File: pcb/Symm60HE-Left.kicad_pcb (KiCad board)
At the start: 2 copper layers, 155.5 x 106.4 mm, 124 parts

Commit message: Rename to Symm60HE; two-layer routing that is clean by construction
Rename every DOE60-* file and reference to Symm60HE-*, matching the repo.
The seven "DOE" mentions that remain are about the layout being reproduced,
which is correct.

Routing is now two layers with vias, at 0.2 mm trace / 0.15 mm clearance /
0.45 mm vias -- a rule chosen so the 0.5 mm grid's own diagonal spacing
(0.354 mm) satisfies it, and relaxed for any fabricator.

Three fixes, each of which was a real defect in the single-layer pass:

  * A diagonal step now requires both of its orthogonal neighbours.  Without
    it two nets cut the same gap from opposite corners and cross; cell
    ownership cannot see that, because neither net owns a cell the other
    used.  It was producing 49 shorts on the left half alone.
  * Fine-pitch pins are met head-on through a private escape lane along the
    pad's own axis, staggered near/far by pin parity.  A 0.65 mm TSSOP has
    0.25 mm between pads, so there is no side access at any rule; and without
    the lane the two neighbours' keep-out margins meet in front of a pin's
    tip and one of them owns the only way out.  The lane runs both ways,
    because an edge connector's contacts face off-board -- that is the way
    the cable goes in -- so its only exit is inwards under its own body.
  * Every route is rebuilt as real geometry and checked against everything
    already on the board before it is kept.  A route that would violate
    clearance is dropped and counted unrouted, so the files on disk are clean
    by construction and the honest number is the routed/unrouted split.

Left 143 of 156 connections, right 151 of 168, daughterboard 15 of 37.

Two things the checks were missing:

  * routecheck.py never tested trace-to-trace clearance, which is exactly
    what the diagonal crossings needed.  It does now, and it no longer counts
    a branch leaving its trunk at a T as a loose end.
  * The USB-C keep-out only existed in the image script -- nothin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
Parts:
- removed AMR1, AMR2, AMR3, AMR4: SN74LV4051A, DOE60_Project:AM1_TSSOP-16_4.4x5mm_P0.65mm
- removed CMR1, CMR2, CMR3, CMR4, CR10A, CR11A, CR12A, CR13A, CR14A, CR15A, CR16A, CR17A, CR18A, CR19A, CR1A, CR20A, CR21A, CR22A, CR23A, CR24A, CR25A, CR26A, CR27A, CR28A, CR29A, CR2A, CR30A, CR31A, CR32A, CR33A, CR34A, CR35A, CR36A, CR3A, CR4A, CR5A, CR6A, CR7A, CR8A, CR9A: 100n, DOE60_Project:C1_C_0402_1005Metric
- removed CR10B, CR11B, CR12B, CR13B, CR14B, CR15B, CR16B, CR17B, CR18B, CR19B, CR1B, CR20B, CR21B, CR22B, CR23B, CR24B, CR25B, CR26B, CR27B, CR28B, CR29B, CR2B, CR30B, CR31B, CR32B, CR33B, CR34B, CR35B, CR36B, CR3B, CR4B, CR5B, CR6B, CR7B, CR8B, CR9B: 4.7n, DOE60_Project:C1_C_0402_1005Metric
- removed HER1, HER10, HER12, HER13, HER14, HER15, HER16, HER17, HER19, HER2, HER20, HER21, HER22, HER23, HER24, HER27, HER28, HER29, HER3, HER30, HER32, HER34, HER5, HER6, HER7, HER8, HER9: MT9102ET, DOE60_Project:HE_KEY_1.00u
- removed HER11, HER31, HER33, HER35: MT9102ET, DOE60_Project:HE_KEY_1.50u
- removed HER18: MT9102ET, DOE60_Project:HE_KEY_1.75u
- removed HER25, HER36: MT9102ET, DOE60_Project:HE_KEY_2.25u
- removed HER26: MT9102ET, DOE60_Project:HE_KEY_1.25u
- removed HER4: MT9102ET, DOE60_Project:HE_KEY_2.00u
- removed JR1: FFC_12P, DOE60_Project:FFC_12P_1.00mm_TopContact
- removed MHR1, MHR2, MHR3, MHR4: M2, DOE60_Project:MountingHole_2.2mm_M2_Pad
- removed SR1, SR2, SR3: STAB_MX, DOE60_Project:STABILIZER_MX_2U
- added AML1: SN74LV4051A, Symm60HE_Project:AM1_TSSOP-16_4.4x5mm_P0.65mm, B.Cu at (23.8, 65.5)
- added AML2: SN74LV4051A, Symm60HE_Project:AM1_TSSOP-16_4.4x5mm_P0.65mm, B.Cu at (55.3, 65.0)
- added AML3: SN74LV4051A, Symm60HE_Project:AM1_TSSOP-16_4.4x5mm_P0.65mm, B.Cu at (91.3, 60.5)
- added AML4: SN74LV4051A, Symm60HE_Project:AM1_TSSOP-16_4.4x5mm_P0.65mm, B.Cu at (116.3, 59.0)
- added CL10A: 100n, Symm60HE_Project:C1_C_0402_1005Metric, B.Cu at (50.5, 21.7)
- added CL10B: 4.7n, Symm60HE_Project:C1_C_0402_1005Metric, B.Cu at (63.8, 35.5)
- added CL11A: 100n, Symm60HE_Project:C1_C_0402_1005Metric, B.Cu at (69.8, 21.7)
- added CL11B: 4.7n, Symm60HE_Project:C1_C_0402_1005Metric, B.Cu at (82.8, 35.7)
- added CL12A: 100n, Symm60HE_Project:C1_C_0402_1005Metric, B.Cu at (90.3, 22.1)
- added CL12B: 4.7n, Symm60HE_Project:C1_C_0402_1005Metric, B.Cu at (102.7, 36.6)
- added CL13A: 100n, Symm60HE_Project:C1_C_0402_1005Metric, B.Cu at (111.8, 23.5)
- added CL13B: 4.7n, Symm60HE_Project:C1_C_0402_1005Metric, B.Cu at (123.5, 38.6)
- added CL14A: 100n, Symm60HE_Project:C1_C_0402_1005Metric, B.Cu at (132.2, 25.7)
- added CL14B: 4.7n, Symm60HE_Project:C1_C_0402_1005Metric, B.Cu at (143.8, 40.9)
- added CL15A: 100n, Symm60HE_Project:C1_C_0402_1005Metric, B.Cu at (9.12, 40.7)
- added CL15B: 4.7n, Symm60HE_Project:C1_C_0402_1005Metric, B.Cu at (22.3, 54.5)
- added CL16A: 100n, Symm60HE_Project:C1_C_0402_1005Metric, B.Cu at (35.3, 40.7)
- added CL16B: 4.7n, Symm60HE_Project:C1_C_0402_1005Metric, B.Cu at (48.5, 54.5)
- added CL17A: 100n, Symm60HE_Project:C1_C_0402_1005Metric, B.Cu at (54.4, 40.7)
- added CL17B: 4.7n, Symm60HE_Project:C1_C_0402_1005Metric, B.Cu at (67.6, 54.5)
- added CL18A: 100n, Symm60HE_Project:C1_C_0402_1005Metric, B.Cu at (73.7, 40.8)
- added CL18B: 4.7n, Symm60HE_Project:C1_C_0402_1005Metric, B.Cu at (86.7, 54.8)
- added CL19A: 100n, Symm60HE_Project:C1_C_0402_1005Metric, B.Cu at (94.6, 41.4)
- added CL19B: 4.7n, Symm60HE_Project:C1_C_0402_1005Metric, B.Cu at (106.9, 56.0)
- added CL1A: 100n, Symm60HE_Project:C1_C_0402_1005Metric, B.Cu at (4.83, 2.62)
- added CL1B: 4.7n, Symm60HE_Project:C1_C_0402_1005Metric, B.Cu at (18.0, 16.4)
- added CL20A: 100n, Symm60HE_Project:C1_C_0402_1005Metric, B.Cu at (116.0, 43.0)
- added CL20B: 4.7n, Symm60HE_Project:C1_C_0402_1005Metric, B.Cu at (127.6, 58.1)
- added CL21A: 100n, Symm60HE_Project:C1_C_0402_1005Metric, B.Cu at (9.12, 59.8)
- added CL21B: 4.7n, Symm60HE_Project:C1_C_0402_1005Metric, B.Cu at (22.3, 73.6)
- added CL22A: 100n, Symm60HE_Project:C1_C_0402_1005Metric, B.Cu at (40.1, 59.8)
- added CL22B: 4.7n, Symm60HE_Project:C1_C_0402_1005Metric, B.Cu at (53.3, 73.6)
- added CL23A: 100n, Symm60HE_Project:C1_C_0402_1005Metric, B.Cu at (59.1, 59.8)
- added CL23B: 4.7n, Symm60HE_Project:C1_C_0402_1005Metric, B.Cu at (72.3, 73.6)
- added CL24A: 100n, Symm60HE_Project:C1_C_0402_1005Metric, B.Cu at (78.8, 59.9)
- added CL24B: 4.7n, Symm60HE_Project:C1_C_0402_1005Metric, B.Cu at (91.6, 74.1)
- added CL25A: 100n, Symm60HE_Project:C1_C_0402_1005Metric, B.Cu at (100.0, 60.7)
- added CL25B: 4.7n, Symm60HE_Project:C1_C_0402_1005Metric, B.Cu at (112.0, 75.5)
- added CL26A: 100n, Symm60HE_Project:C1_C_0402_1005Metric, B.Cu at (121.2, 62.6)
- added CL26B: 4.7n, Symm60HE_Project:C1_C_0402_1005Metric, B.Cu at (132.8, 77.8)
- added CL27A: 100n, Symm60HE_Project:C1_C_0402_1005Metric, B.Cu at (1.97, 78.8)
- added CL27B: 4.7n, Symm60HE_Project:C1_C_0402_1005Metric, B.Cu at (15.2, 92.6)
- added CL28A: 100n, Symm60HE_Project:C1_C_0402_1005Metric, B.Cu at (6.74, 78.8)
- added CL28B: 4.7n, Symm60HE_Project:C1_C_0402_1005Metric, B.Cu at (19.9, 92.6)
- added CL29A: 100n, Symm60HE_Project:C1_C_0402_1005Metric, B.Cu at (21.0, 78.8)
- added CL29B: 4.7n, Symm60HE_Project:C1_C_0402_1005Metric, B.Cu at (34.2, 92.6)
- added CL2A: 100n, Symm60HE_Project:C1_C_0402_1005Metric, B.Cu at (23.9, 2.62)
- added CL2B: 4.7n, Symm60HE_Project:C1_C_0402_1005Metric, B.Cu at (37.1, 16.4)
- added CL30A: 100n, Symm60HE_Project:C1_C_0402_1005Metric, B.Cu at (35.3, 78.8)
- added CL30B: 4.7n, Symm60HE_Project:C1_C_0402_1005Metric, B.Cu at (48.5, 92.6)
- added CL31A: 100n, Symm60HE_Project:C1_C_0402_1005Metric, B.Cu at (40.1, 78.8)
- added CL31B: 4.7n, Symm60HE_Project:C1_C_0402_1005Metric, B.Cu at (53.3, 92.6)
- added CL32A: 100n, Symm60HE_Project:C1_C_0402_1005Metric, B.Cu at (78.7, 79.1)
- added CL32B: 4.7n, Symm60HE_Project:C1_C_0402_1005Metric, B.Cu at (91.4, 93.3)
- added CL33A: 100n, Symm60HE_Project:C1_C_0402_1005Metric, B.Cu at (117.2, 81.4)
- added CL33B: 4.7n, Symm60HE_Project:C1_C_0402_1005Metric, B.Cu at (128.9, 96.5)
- added CL3A: 100n, Symm60HE_Project:C1_C_0402_1005Metric, B.Cu at (42.9, 2.62)
- added CL3B: 4.7n, Symm60HE_Project:C1_C_0402_1005Metric, B.Cu at (56.1, 16.4)
- added CL4A: 100n, Symm60HE_Project:C1_C_0402_1005Metric, B.Cu at (62.0, 2.63)
- added CL4B: 4.7n, Symm60HE_Project:C1_C_0402_1005Metric, B.Cu at (75.2, 16.5)
- added CL5A: 100n, Symm60HE_Project:C1_C_0402_1005Metric, B.Cu at (81.9, 2.79)
- added CL5B: 4.7n, Symm60HE_Project:C1_C_0402_1005Metric, B.Cu at (94.6, 17.1)
- added CL6A: 100n, Symm60HE_Project:C1_C_0402_1005Metric, B.Cu at (103.2, 3.78)
- added CL6B: 4.7n, Symm60HE_Project:C1_C_0402_1005Metric, B.Cu at (115.2, 18.7)
- added CL7A: 100n, Symm60HE_Project:C1_C_0402_1005Metric, B.Cu at (124.3, 5.75)
- added CL7B: 4.7n, Symm60HE_Project:C1_C_0402_1005Metric, B.Cu at (135.9, 21.0)
- added CL8A: 100n, Symm60HE_Project:C1_C_0402_1005Metric, B.Cu at (7.69, 21.7)
- added CL8B: 4.7n, Symm60HE_Project:C1_C_0402_1005Metric, B.Cu at (20.9, 35.5)
- added CL9A: 100n, Symm60HE_Project:C1_C_0402_1005Metric, B.Cu at (31.5, 21.7)
- added CL9B: 4.7n, Symm60HE_Project:C1_C_0402_1005Metric, B.Cu at (44.7, 35.5)
- added CML1: 100n, Symm60HE_Project:C1_C_0402_1005Metric, B.Cu at (31.3, 65.0)
- added CML2: 100n, Symm60HE_Project:C1_C_0402_1005Metric, B.Cu at (62.3, 63.0)
- added CML3: 100n, Symm60HE_Project:C1_C_0402_1005Metric, B.Cu at (98.3, 59.0)
- added CML4: 100n, Symm60HE_Project:C1_C_0402_1005Metric, B.Cu at (123.3, 59.0)
- added HEL1: MT9102ET, Symm60HE_Project:HE_KEY_1.00u, B.Cu at (11.4, 9.53)
- added HEL10: MT9102ET, Symm60HE_Project:HE_KEY_1.00u, B.Cu at (57.1, 28.6)
- added HEL11: MT9102ET, Symm60HE_Project:HE_KEY_1.00u, B.Cu at (76.3, 28.7)
- added HEL12: MT9102ET, Symm60HE_Project:HE_KEY_1.00u, B.Cu at (96.5, 29.4)
- added HEL13: MT9102ET, Symm60HE_Project:HE_KEY_1.00u, B.Cu at (117.6, 31.1)
- added HEL14: MT9102ET, Symm60HE_Project:HE_KEY_1.00u, B.Cu at (138.0, 33.3)
- added HEL15: MT9102ET, Symm60HE_Project:HE_KEY_1.75u, B.Cu at (15.7, 47.6)
- added HEL16: MT9102ET, Symm60HE_Project:HE_KEY_1.00u, B.Cu at (41.9, 47.6)
- added HEL17: MT9102ET, Symm60HE_Project:HE_KEY_1.00u, B.Cu at (61.0, 47.6)
- added HEL18: MT9102ET, Symm60HE_Project:HE_KEY_1.00u, B.Cu at (80.2, 47.8)
- added HEL19: MT9102ET, Symm60HE_Project:HE_KEY_1.00u, B.Cu at (100.7, 48.7)
- added HEL2: MT9102ET, Symm60HE_Project:HE_KEY_1.00u, B.Cu at (30.5, 9.53)
- added HEL20: MT9102ET, Symm60HE_Project:HE_KEY_1.00u, B.Cu at (121.8, 50.5)
- added HEL21: MT9102ET, Symm60HE_Project:HE_KEY_2.25u, B.Cu at (15.7, 66.7)
- added HEL22: MT9102ET, Symm60HE_Project:HE_KEY_1.00u, B.Cu at (46.7, 66.7)
- added HEL23: MT9102ET, Symm60HE_Project:HE_KEY_1.00u, B.Cu at (65.7, 66.7)
- added HEL24: MT9102ET, Symm60HE_Project:HE_KEY_1.00u, B.Cu at (85.2, 67.0)
- added HEL25: MT9102ET, Symm60HE_Project:HE_KEY_1.00u, B.Cu at (106.0, 68.1)
- added HEL26: MT9102ET, Symm60HE_Project:HE_KEY_1.00u, B.Cu at (127.0, 70.2)
- added HEL27: MT9102ET, Symm60HE_Project:HE_KEY_1.00u, B.Cu at (8.57, 85.7)
- added HEL28: MT9102ET, Symm60HE_Project:HE_KEY_1.50u, B.Cu at (13.3, 85.7)
- added HEL29: MT9102ET, Symm60HE_Project:HE_KEY_1.00u, B.Cu at (27.6, 85.7)
- added HEL3: MT9102ET, Symm60HE_Project:HE_KEY_1.00u, B.Cu at (49.5, 9.53)
- added HEL30: MT9102ET, Symm60HE_Project:HE_KEY_1.50u, B.Cu at (41.9, 85.7)
- added HEL31: MT9102ET, Symm60HE_Project:HE_KEY_1.00u, B.Cu at (46.7, 85.7)
- added HEL32: MT9102ET, Symm60HE_Project:HE_KEY_1.50u, B.Cu at (85.1, 86.2)
- added HEL33: MT9102ET, Symm60HE_Project:HE_KEY_2.25u, B.Cu at (123.0, 89.0)
- added HEL4: MT9102ET, Symm60HE_Project:HE_KEY_1.00u, B.Cu at (68.6, 9.55)
- added HEL5: MT9102ET, Symm60HE_Project:HE_KEY_1.00u, B.Cu at (88.3, 9.93)
- added HEL6: MT9102ET, Symm60HE_Project:HE_KEY_1.00u, B.Cu at (109.2, 11.2)
- added HEL7: MT9102ET, Symm60HE_Project:HE_KEY_1.00u, B.Cu at (130.1, 13.3)
- added HEL8: MT9102ET, Symm60HE_Project:HE_KEY_1.50u, B.Cu at (14.3, 28.6)
- added HEL9: MT9102ET, Symm60HE_Project:HE_KEY_1.00u, B.Cu at (38.1, 28.6)
- added JL1: FFC_12P, Symm60HE_Project:FFC_12P_1.00mm_TopContact, B.Cu at (136.3, 45.0)
- added MHL1: M2, Symm60HE_Project:MountingHole_2.2mm_M2_Pad, F.Cu at (4.79, 10.0)
- added MHL2: M2, Symm60HE_Project:MountingHole_2.2mm_M2_Pad, F.Cu at (3.29, 92.0)
- added MHL3: M2, Symm60HE_Project:MountingHole_2.2mm_M2_Pad, F.Cu at (136.8, 10.0)
- added MHL4: M2, Symm60HE_Project:MountingHole_2.2mm_M2_Pad, F.Cu at (136.3, 89.5)
- added SL1: STAB_MX, Symm60HE_Project:STABILIZER_MX_2U, F.Cu at (15.7, 66.7)
- added SL2: STAB_MX, Symm60HE_Project:STABILIZER_MX_2U, F.Cu at (123.0, 89.0)
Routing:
- net +3V3A: track 336.9 -> 914.8 mm, vias 33 -> 42
- net HE_L07: track 0.00 -> 139.2 mm, vias 0 -> 4
- net HE_L27: track 0.00 -> 136.6 mm, vias 0 -> 2
- net MUX_A0: track 0.00 -> 128.9 mm, vias 0 -> 6
- net ADC_L1: track 0.00 -> 124.1 mm, vias 0 -> 4
- net HE_L06: track 0.00 -> 124.1 mm, vias 0 -> 4
- net HE_L28: track 0.00 -> 119.2 mm, vias 0 -> 2
- net HE_L14: track 0.00 -> 112.0 mm, vias 0 -> 2
- net ADC_L2: track 0.00 -> 92.6 mm, vias 0 -> 2
- net HE_L29: track 0.00 -> 87.5 mm, vias 0 -> 2
- net HE_L13: track 0.00 -> 87.1 mm, vias 0 -> 2
- net HE_L21: track 0.00 -> 84.9 mm, vias 0 -> 2
- net HE_L03: track 0.00 -> 76.1 mm
- net HE_L12: track 0.00 -> 68.1 mm, vias 0 -> 2
- net ADC_L3: track 0.00 -> 61.0 mm
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- added copper zone on F.Cu, net GND
- removed copper zone on F.Cu, net +3V3A
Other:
- board size 155.5 x 106.4 mm -> 157.9 x 105.9 mm

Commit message: Get the boards routing: SOIC muxes, FN40HE's pinout, a rail plane
Four changes, none of which touch what the circuit is made of.

SOIC-16 muxes.  FN40HE fits the SN74LV4051A in TSSOP-16, and every remaining
failure on the halves was an interior pin of one.  A 0.65 mm pitch leaves
0.25 mm between pads: no trace fits between them at any rule a fabricator
will take, so those pins could only ever escape by via through a gap their
neighbours already owned.  Same chip in SOIC-16 -- SN74LV4051AD -- has
1.27 mm pitch and 0.67 mm between pads, which a 0.2 mm trace clears with
0.15 mm either side.  It costs about 30 mm2 a package on boards that have
room under the keycaps, and it hand solders.

The MCU pin assignment is FN40HE's again, read off its board: crystal on
5/6, reset on 7, the mux selects on 9/10/11, the analog rail on 13, the
eight multiplexed inputs on 17 and 20-26, USB and its reference resistor on
33/34/35, SWD on 46/49/55, boot on 60.  The previous commit had moved those
around to suit the layout, which is backwards -- most of them are fixed in
silicon.  The parts move instead.  NOTICE.md is corrected accordingly.

The analog rail is a pour, not a net.  It reaches 75 pads on the left half;
routed as traces it is a spanning tree that gets there first and walls off
the three select lines, which have one shape that works.  F.Cu carries it
instead -- the halves have no components on the front -- and each rail pad
taps it through a via of its own.  That is FN40HE's +3.3VA zone, on the
other side because our board is populated the other way up.  B.Cu stays the
GND pour, so neither rail is routed.

And the one that mattered most: a pad's list of ways to be met had the bare
pad centre first.  Meeting a pad in its middle lets the maze leave sideways,
which on a 0.5 mm pitch package crosses the neighbouring pin, so all twelve
of those candidates were found and then thrown out by the clearance check --
exhausting the per-pad budget before the escapes along the pad's own a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
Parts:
- AML1, AML2, AML3, AML4: footprint Symm60HE_Project:AM1_TSSOP-16_4.4x5mm_P0.65mm -> Symm60HE_Project:AM1_SOIC-16_3.9x9.9mm_P1.27mm
- moved CML4 19.4 mm to (142.3, 63.0)
- moved AML4 18.4 mm to (134.3, 63.0)
- moved AML1 13.9 mm to (29.8, 53.0)
- moved CML1 13.3 mm to (37.0, 53.0)
- moved AML3 7.62 mm to (94.3, 67.5)
- moved CML3 6.40 mm to (102.3, 64.0)
- moved MHL4 5.85 mm to (141.8, 91.5)
- moved CML2 4.12 mm to (63.3, 59.0)
- moved AML2 0.50 mm to (55.8, 65.0)
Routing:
- net +3V3A: track 914.8 -> 112.7 mm, vias 42 -> 66
- net MUX_A1: track 0.19 -> 131.4 mm, vias 0 -> 4
- net HE_L07: track 139.2 -> 13.1 mm, vias 4 -> 0
- net ADC_L1: track 124.1 -> 0.00 mm, vias 4 -> 0
- net MUX_A2: track 0.26 -> 121.8 mm, vias 0 -> 5
- net HE_L05: track 9.37 -> 96.4 mm
- net ADC_L3: track 61.0 -> 0.00 mm
- net HE_L27: track 136.6 -> 165.2 mm, vias 2 -> 0
- net HE_L28: track 119.2 -> 145.6 mm
- net HE_L29: track 87.5 -> 110.4 mm
- net HE_L25: track 26.6 -> 44.7 mm, vias 0 -> 3
- net HE_L16: track 27.0 -> 13.2 mm
- net HE_L03: track 76.1 -> 62.9 mm
- net HE_L02: track 60.6 -> 48.0 mm
- net HE_L21: track 84.9 -> 96.0 mm, vias 2 -> 0
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- added copper zone on F.Cu, net +3V3A
- removed copper zone on F.Cu, net GND

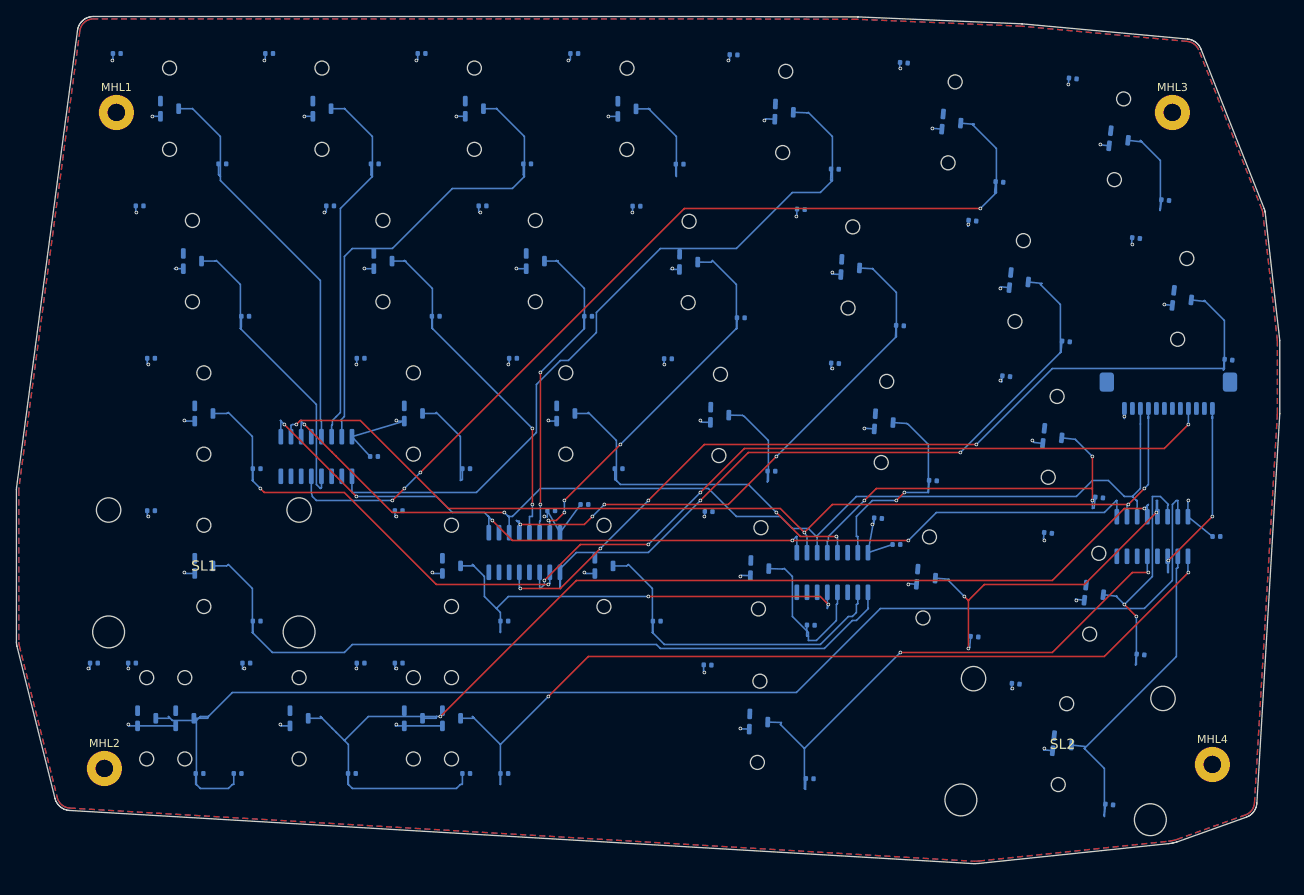
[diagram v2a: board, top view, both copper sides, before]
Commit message: Replace repo contents with current Symm60HE project folder
Adds firmware (libhmk), release fabrication outputs, pogo/neo PCB variants,
Fusion 360 case sources, and updated docs/tools.

Co-Authored-By: Claude Opus 5 <noreply@anthropic.com>
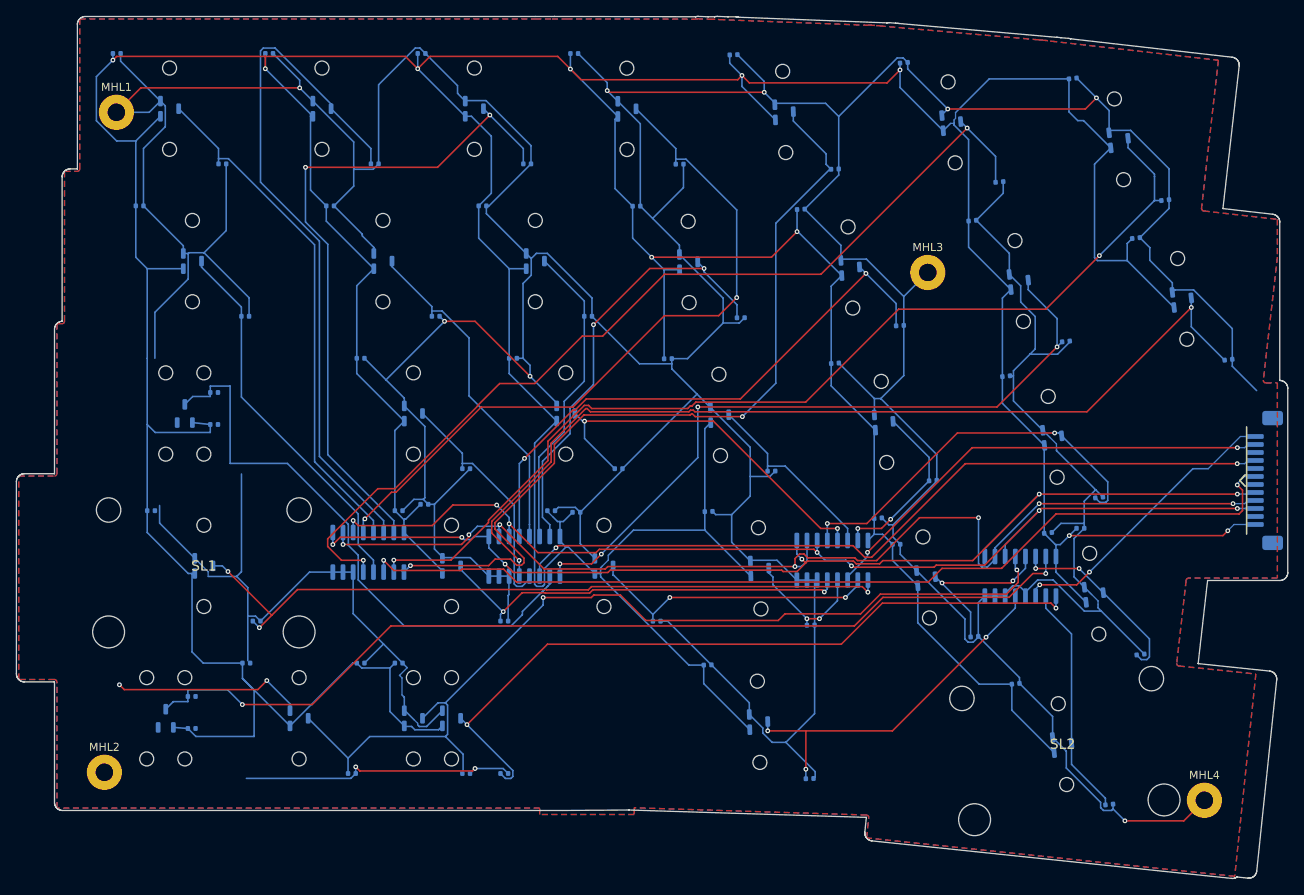
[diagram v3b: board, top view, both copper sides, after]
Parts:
- removed CL28A: 100n, Symm60HE_Project:C1_C_0402_1005Metric
- removed CL28B: 4.7n, Symm60HE_Project:C1_C_0402_1005Metric
- removed HEL28: MT9102ET, Symm60HE_Project:HE_KEY_1.50u
- added KML15N, KML15S: MX_MECHANICAL_ONLY, HE_KEY_MECHANICAL_ONLY, B.Cu at (15.7, 47.6)
- added KML27A: MX_MECHANICAL_ONLY, HE_KEY_MECHANICAL_ONLY, B.Cu at (13.3, 85.7)
- added KML27N: MX_MECHANICAL_ONLY, HE_KEY_MECHANICAL_ONLY, B.Cu at (8.57, 85.7)
- HEL1, HEL10, HEL11, HEL12, HEL13, HEL14, HEL16, HEL17, HEL18, HEL19, HEL2, HEL20, HEL22, HEL23, HEL24, HEL25, HEL26, HEL29, HEL3, HEL31, HEL4, HEL5, HEL6, HEL7, HEL9: footprint Symm60HE_Project:HE_KEY_1.00u -> HE_KEY_1.00u
- HEL15: footprint Symm60HE_Project:HE_KEY_1.75u -> HE_SHARED_MIDPOINT
- HEL21, HEL33: footprint Symm60HE_Project:HE_KEY_2.25u -> HE_KEY_2.25u
- HEL27: footprint Symm60HE_Project:HE_KEY_1.00u -> HE_SHARED_MIDPOINT
- HEL30, HEL32, HEL8: footprint Symm60HE_Project:HE_KEY_1.50u -> HE_KEY_1.50u
- moved MHL3 36.5 mm to (106.2, 30.0)
- moved AML4 17.2 mm to (117.8, 68.0)
- moved CML4 17.0 mm to (125.3, 62.0)
- moved JL1 16.2 mm to (148.2, 56.0), turned to -90 degrees
- moved CL27A 14.7 mm to (14.2, 87.0)
- moved AML1 13.6 mm to (36.3, 65.0)
- moved CL15A 11.4 mm to (17.0, 49.0)
- moved CL15B 10.9 mm to (17.0, 45.0)
- moved CL27B 9.67 mm to (14.2, 83.0)
- moved CML1 8.68 mm to (43.3, 59.0)
- moved MHL4 4.59 mm to (140.8, 96.0)
- moved HEL15 2.38 mm to (13.3, 47.6), turned to 90 degrees
- moved HEL27 2.38 mm to (11.0, 85.7), turned to 90 degrees
- moved AML3 1.52 mm to (94.3, 66.0)
- moved CML2 1.40 mm to (62.3, 60.0)
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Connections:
- JL1 pad 1: +3V3A -> ADC_L4
- JL1 pad 10: GND -> MUX_A0
- JL1 pad 11: ADC_L3 -> GND
- JL1 pad 12: ADC_L4 -> +3V3A
- JL1 pad 2: GND -> ADC_L3
- JL1 pad 3: MUX_A0 -> GND
- JL1 pad 4: MUX_A1 -> ADC_L2
- JL1 pad 5: MUX_A2 -> GND
- JL1 pad 6: GND -> ADC_L1
- JL1 pad 7: ADC_L1 -> GND
- JL1 pad 8: GND -> MUX_A2
- JL1 pad 9: ADC_L2 -> MUX_A1
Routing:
- net GND: track 0.00 -> 1037.8 mm, vias 0 -> 12
- net +3V3A: track 112.7 -> 845.1 mm, vias 66 -> 10
- net ADC_L1: track 0.00 -> 119.1 mm, vias 0 -> 2
- net HE_L07: track 13.1 -> 127.2 mm, vias 0 -> 2
- net HE_L04: track 13.4 -> 89.9 mm, vias 0 -> 2
- net ADC_L3: track 0.00 -> 57.6 mm, vias 0 -> 2
- net HE_L27: track 165.2 -> 121.5 mm, vias 0 -> 2
- net HE_L02: track 48.0 -> 88.0 mm
- net HE_L28: track 145.6 -> 120.3 mm
- net HE_L25: track 44.7 -> 22.1 mm, vias 3 -> 2
- net HE_L03: track 62.9 -> 84.9 mm, vias 0 -> 2
- net HE_L30: track 67.0 -> 45.9 mm, vias 2 -> 3
- net HE_L16: track 13.2 -> 30.2 mm
- net HE_L29: track 110.4 -> 93.6 mm
- net MUX_A2: track 121.8 -> 137.7 mm, vias 5 -> 6
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- added copper zone on F.Cu, net GND
- removed copper zone on F.Cu, net +3V3A
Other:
- board size 157.9 x 105.9 mm -> 158.9 x 107.8 mm
